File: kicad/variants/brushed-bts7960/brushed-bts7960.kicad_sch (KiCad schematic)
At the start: 70 parts, among them IC1 rp2040_RP2040_breakout_swd, J1 HDR-M-2.54_1x3, J2 HDR-M-2.54_1x4, J3 HDR-M-2.54_1x4, J4 HDR-M-2.54_1x4, U1 SN74AHC244DW, U2 BTN7970, U3 BTN7970, U4 BTN7970, U5 BTN7970, U6 BMI160, U7 SPX3819M5-L-3-3/TR

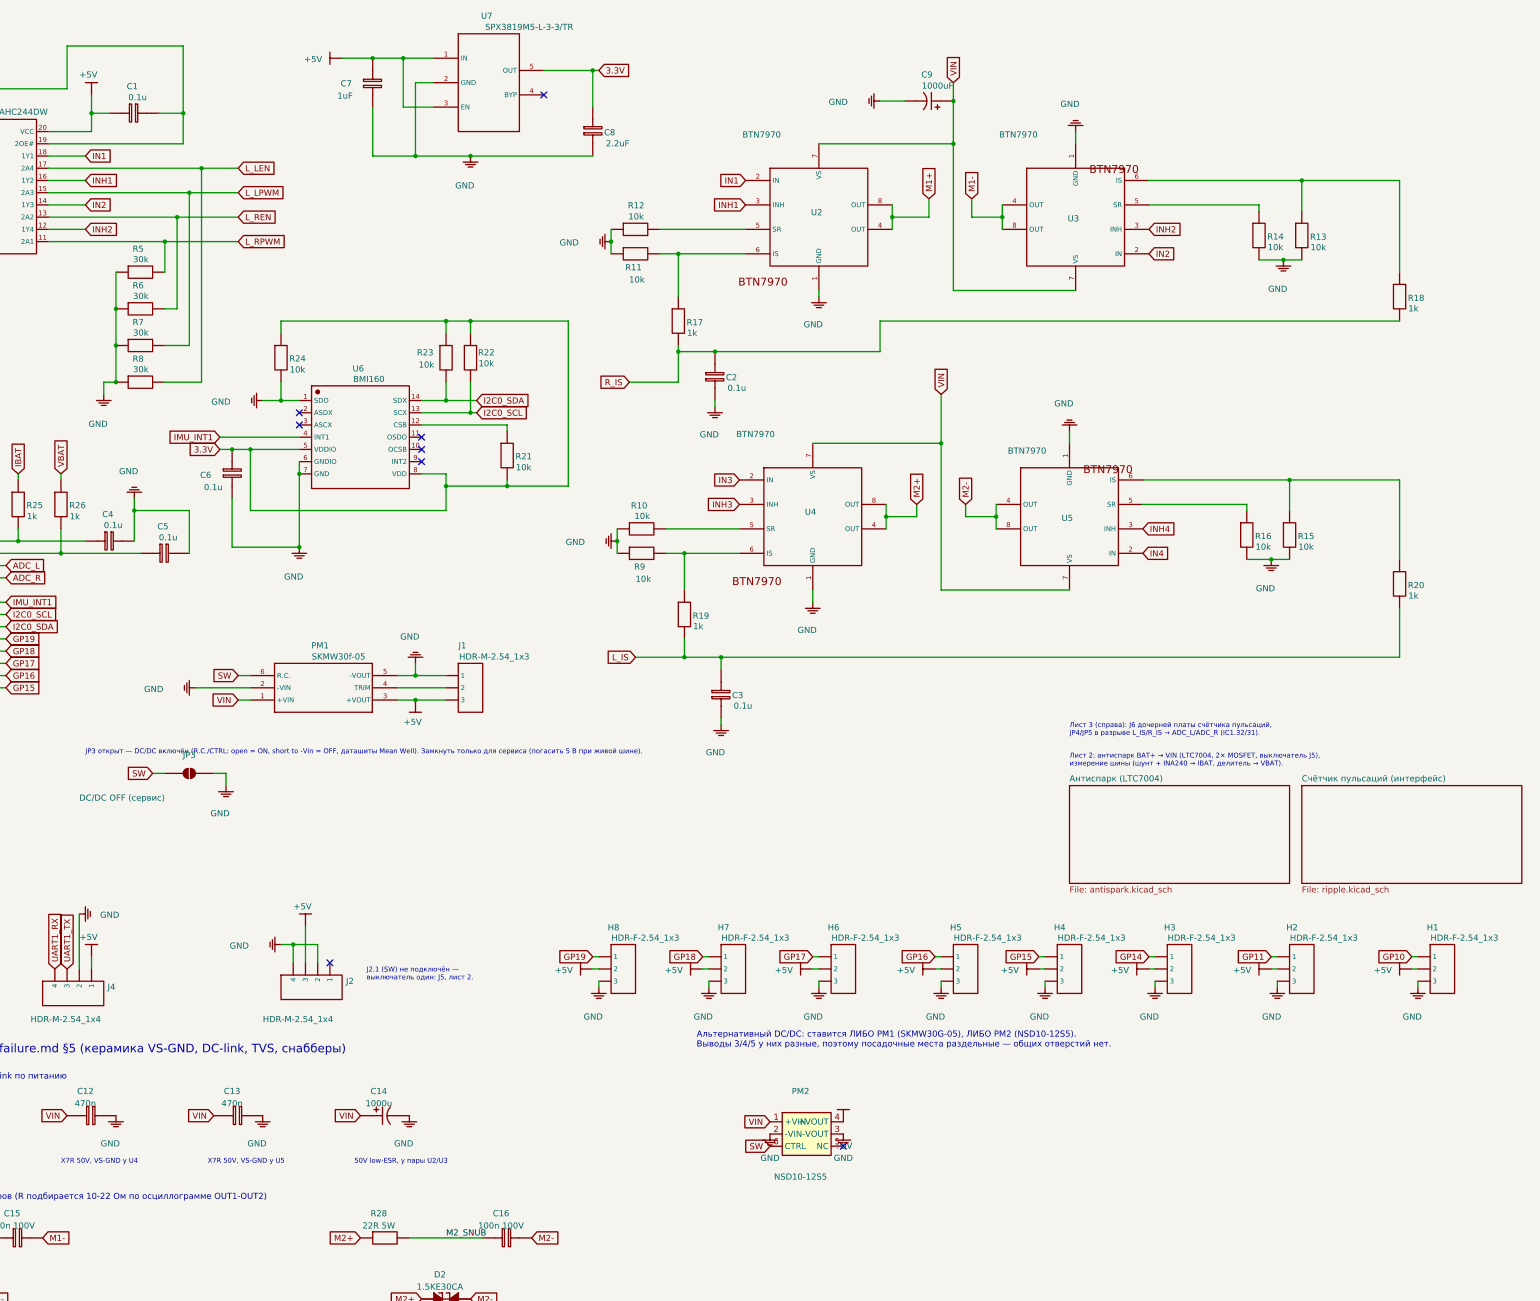
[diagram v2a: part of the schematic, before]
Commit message: feat(kicad): перенос силовых клемм, DC/DC и антиспарка на плату + скрипт Update PCB from Schematic
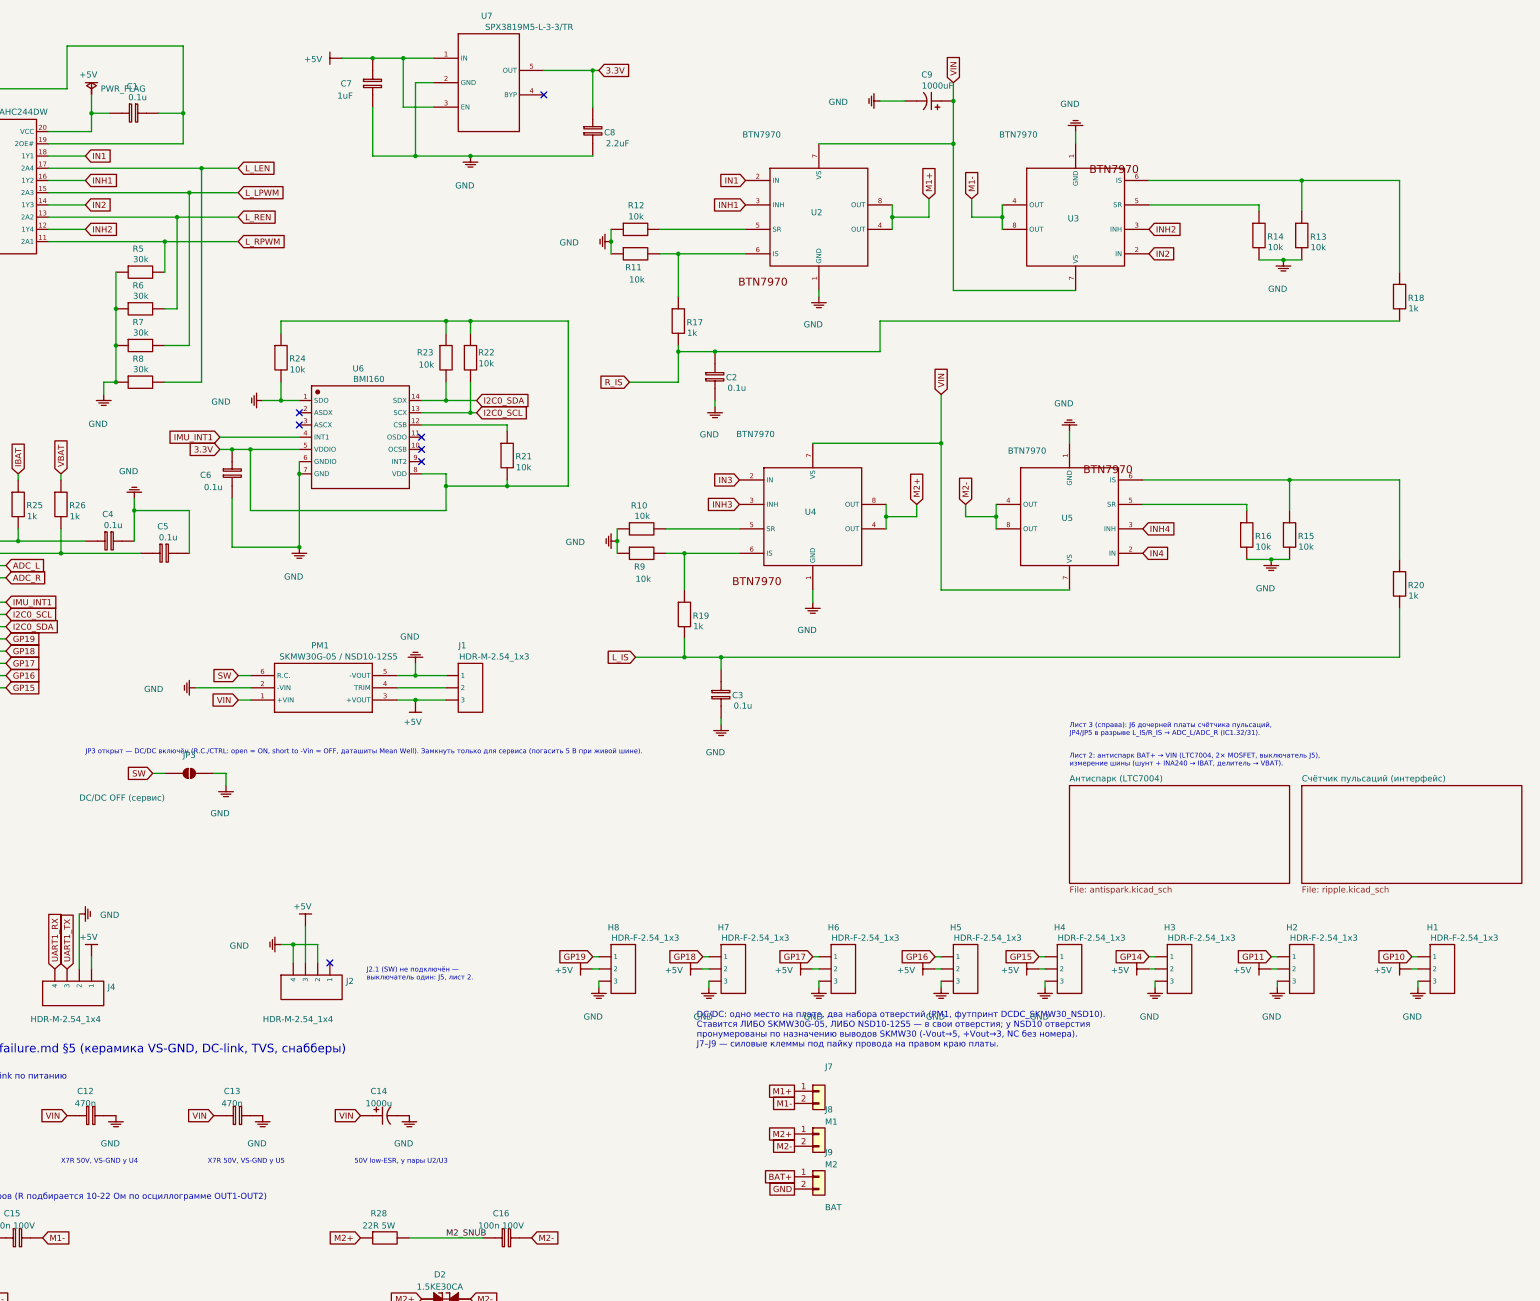
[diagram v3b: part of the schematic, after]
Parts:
- removed PM2: NSD10-12S5, Converter_DCDC:Converter_DCDC_MeanWell_NSD10_THT, symbol biba:NSD10
- added J7: M1, biba:WirePad_1x2_P7.62mm_D2.0mm, symbol Connector_Generic:Conn_01x02
- added J8: M2, biba:WirePad_1x2_P7.62mm_D2.0mm, symbol Connector_Generic:Conn_01x02
- added J9: BAT, biba:WirePad_1x2_P7.62mm_D2.0mm, symbol Connector_Generic:Conn_01x02
- PM1: value SKMW30f-05 -> SKMW30G-05 / NSD10-12S5; footprint biba:SKMW30G-05 -> biba:DCDC_SKMW30_NSD10; Package SKMW30G-05 -> SKMW30G-05 или NSD10-12S5
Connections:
- net GND: now also J9.2 (Pin_2)
- net M1+: now also J7.1 (Pin_1)
- net M1-: now also J7.2 (Pin_2)
- net M2+: now also J8.1 (Pin_1)
- net M2-: now also J8.2 (Pin_2)
- new net BAT+: J9.1 (Pin_1)
- no-connect marks 15 -> 14
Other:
- note added: "DC/DC: одно место на плате, два набора отверстий (PM1, футпринт DCDC_SKMW30_NSD10). Ставится ЛИБО SKMW30G-05, ЛИБО NSD10-12S5 — в свои отверстия; у NSD10 отверстия пронумерованы по назначению выводов SKMW30 (-Vout→5, +Vout→3, NC без номера). J7–J9 — силовые клеммы под пайку провода на правом краю платы."
- note removed: "Альтернативный DC/DC: ставится ЛИБО PM1 (SKMW30G-05), ЛИБО PM2 (NSD10-12S5). Выводы 3/4/5 у них разные, поэтому посадочные места раздельные — общих отверстий нет."
